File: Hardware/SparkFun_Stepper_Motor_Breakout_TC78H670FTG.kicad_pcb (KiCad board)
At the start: 4 copper layers, 15.2 x 20.3 mm, 44 parts, among them J1 Conn_01x08, J2 Conn_01x08, U1 TC78H670FTG

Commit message: version to v10
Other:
- board text added: "v10"
- board text removed: "v01"
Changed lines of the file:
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@@
     (effects (font (size 0.5 0.5) (thickness 0.1) bold) (justify left bottom))
   )
-  (gr_text "v01" (at 141.988553 94.318209 180) (layer "B.Cu")
+  (gr_text "v10" (at 141.988553 94.318209 180) (layer "B.Cu")
     (effects (font (size 1 1) (thickness 0.15)) (justify left bottom mirror))
   )

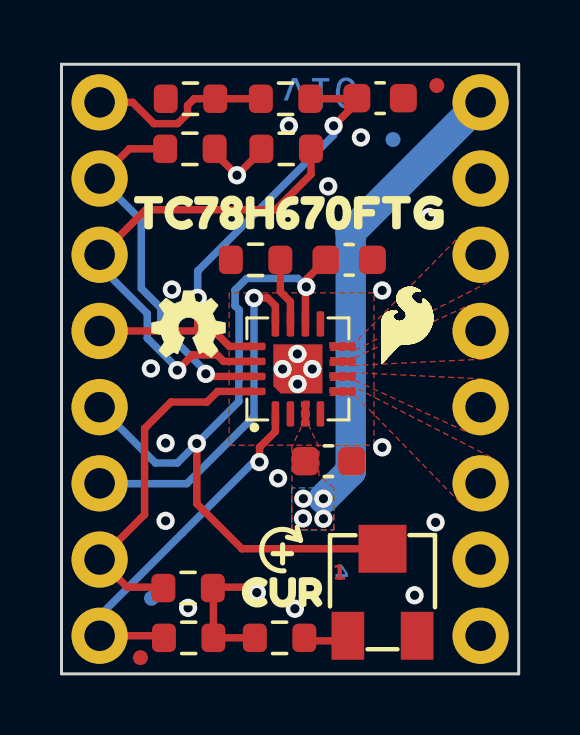
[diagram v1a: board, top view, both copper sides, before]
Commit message: library work and sch cleanup
-moved to a 0.05" grid for schematic and tightened things up (made all nets shorter to match smaller grid and only use a single grid space to extend out from any pin)
-updated ordering instructions fp to avoid sch->brd update error
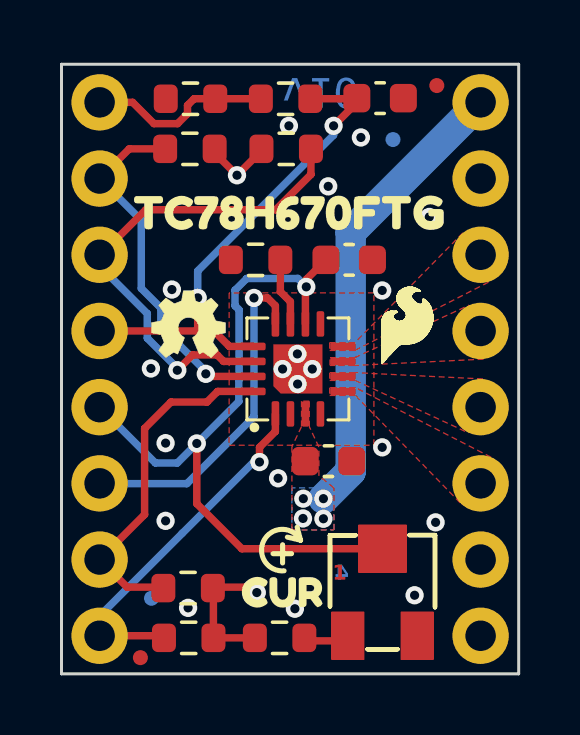
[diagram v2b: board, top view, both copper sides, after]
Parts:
- added R2: 10k, SparkFun-Resistor:Trimpot_SMD_3.0x3.0mm, F.Cu at (145.3, 111.6)
- J1: footprint SparkFun-Connector:1X08 -> SparkFun-Connector:1x08
- U2: footprint SparkFun-Aesthetic:ORDERING_INSTRUCTIONS -> SparkFun-Aesthetic:Ordering_Instructions
- moved U2 2.46 mm to (167.6, 58.5)
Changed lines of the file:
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@@
     )
   )
+  (footprint "SparkFun-Aesthetic:Ordering_Instructions" (layer "F.Cu")
+    (at 167.5642 58.505)
+    (property "Sheetfile" "SparkFun_Stepper_Motor_Breakout_TC78H670FTG.kicad_sch")
+    (property "Sheetname" "")
+    (fp_text reference "U2" (at 2.54 -1.27) (layer "F.Fab") hide
+        (effects (font (size 1.27 1.27) (thickness 0.15)))
+    )
+    (fp_text value "~" (at 2.54 -2.54) (layer "F.Fab") hide
+        (effects (font (size 1.27 1.27) (thickness 0.15)))
+    )
+    (fp_text user "Ordering Instructions:" (at 1.27 1.27) (layer "User.1")
+        (effects (font (size 2.5908 2.5908) (thickness 0.4572)) (justify left top))
+    )
+    (fp_line (start 0 4.445) (end 63.5 4.445)
+      (stroke (width 0.2032) (type solid)) (layer "User.1"))
+    (fp_rect (start 0 0) (end 63.5 50.8)
+      (stroke (width 0.2) (type default)) (fill none) (layer "User.1"))
+  )
   (footprint "SparkFun-Capacitor:C_0603_1608Metric" (layer "F.Cu")
     (at 145.24 95.11)
@@
     )
   )
-  (footprint "SparkFun-Aesthetic:ORDERING_INSTRUCTIONS" (layer "F.Cu")
-    (at 167.64 60.96)
-    (property "Sheetfile" "SparkFun_Stepper_Motor_Breakout_TC78H670FTG.kicad_sch")
-    (property "Sheetname" "")
-    (fp_text reference "U2" (at 2.54 -1.27) (layer "F.Fab") hide
-        (effects (font (size 1.27 1.27) (thickness 0.15)))
-    )
-    (fp_text value "~" (at 2.54 -2.54) (layer "F.Fab") hide
-        (effects (font (size 1.27 1.27) (thickness 0.15)))
-    )
-    (fp_text user "Ordering Instructions:" (at 1.27 1.27) (layer "User.1")
-        (effects (font (size 2.5908 2.5908) (thickness 0.4572)) (justify left top))
-    )
-    (fp_line (start 0 4.445) (end 63.5 4.445)
-      (stroke (width 0.2032) (type solid)) (layer "User.1"))
-    (fp_rect (start 0 0) (end 63.5 50.8)
-      (stroke (width 0.2) (type default)) (fill none) (layer "User.1"))
-  )
   (footprint "SparkFun-Capacitor:C_0603_1608Metric" (layer "F.Cu")
     (at 143.52 107.21)
@@
     )
   )
+  (footprint "SparkFun-Resistor:Trimpot_SMD_3.0x3.0mm" (layer "F.Cu")
+    (at 145.32 111.58)
+    (descr "https://www.ttelectronics.com/TTElectronics/media/ProductFiles/Datasheet/22.pdf")
+    (tags "Trimmer")
+    (property "Mfg Part#" "22AR10K")
+    (property "PROD_ID" "RES-09285")
+    (property "Sheetfile" "SparkFun_Stepper_Motor_Breakout_TC78H670FTG.kicad_sch")
+    (property "Sheetname" "")
+    (property "ki_description" "Potentiometer TRIMPOT-SMD-3MM-CLOSED-1/8W-20%")
+    (property "ki_keywords" "resistor variable trimmer")
+    (attr smd)
+    (fp_text reference "R2" (at 0 -2.8) (layer "F.Fab")
+        (effects (font (size 0.5 0.5) (thickness 0.1) bold))
+    )
+    (fp_text value "10k" (at 0.025 2.875) (layer "F.Fab")
+        (effects (font (size 0.5 0.5) (thickness 0.1) bold))
+    )
+    (fp_line (start -1.75 -1.9) (end -0.9 -1.9)
+      (stroke (width 0.15) (type default)) (layer "F.SilkS"))
+    (fp_line (start -1.75 0.475) (end -1.75 -1.9)
+      (stroke (width 0.15) (type default)) (layer "F.SilkS"))
+    (fp_line (start 0.5 1.9) (end -0.5 1.9)
+      (stroke (width 0.15) (type default)) (layer "F.SilkS"))
+    (fp_line (start 1.75 -1.905) (end 0.9 -1.905)
+      (stroke (width 0.15) (type default)) (layer "F.SilkS"))
+    (fp_line (start 1.75 0.5) (end 1.75 -1.9)
+      (stroke (width 0.15) (type default)) (layer "F.SilkS"))
+    (fp_rect (start -1.875 -2.37) (end 1.875 2.37)
+      (stroke (width 0.05) (type default)) (fill none) (layer "F.CrtYd"))
+    (fp_rect (start -1.6 -1.755) (end 1.6 1.755)
+      (stroke (width 0.1) (type solid)) (fill none) (layer "F.Fab"))
+    (pad "1" smd rect (at -1.155 1.45) (size 1.09 1.6) (layers "F.Cu" "F.Paste" "F.Mask")
+      (net 16 "Net-(R1-Pad2)") (pintype "passive") (thermal_bridge_angle 0))
+    (pad "2" smd rect (at 0 -1.45) (size 1.6 1.6) (layers "F.Cu" "F.Paste" "F.Mask")
+      (net 6 "VREF") (pintype "passive") (thermal_bridge_angle 0))
+    (pad "3" smd rect (at 1.155 1.45) (size 1.09 1.6) (layers "F.Cu" "F.Paste" "F.Mask")
+      (net 13 "GND") (pintype "passive") (thermal_bridge_angle 0))
+  )
   (footprint "SparkFun-Aesthetic:Creative_Commons_License" (layer "F.Cu")
     (at 0.25 0.25)
@@
       (stroke (width 0) (type solid)) (fill solid) (layer "F.SilkS"))
   )
-  (footprint "SparkFun-Connector:1X08" (layer "F.Cu")
+  (footprint "SparkFun-Connector:1x08" (layer "F.Cu")
     (at 135.89 95.25 -90)
     (property "Sheetfile" "SparkFun_Stepper_Motor_Breakout_TC78H670FTG.kicad_sch")
@@
     (property "ki_description" "Generic connector, single row, 01x08, script generated (kicad-library-utils/schlib/autogen/connector/)")
     (property "ki_keywords" "connector")
-    (fp_text reference "J1" (at -1.27 -1.397 90) (layer "F.Fab")
-        (effects (font (size 0.5 0.5) (thickness 0.1)) (justify right bottom))
+    (fp_text reference "J1" (at -1.27 -1.397 -90) (layer "F.Fab")
+        (effects (font (size 0.5 0.5) (thickness 0.1)) (justify left bottom))
     )
-    (fp_text value "Conn_01x08" (at -1.016 1.778 90) (layer "F.Fab")
-        (effects (font (size 0.5 0.5) (thickness 0.1)) (justify right bottom))
+    (fp_text value "Conn_01x08" (at -1.27 2.032 -90) (layer "F.Fab")
+        (effects (font (size 0.5 0.5) (thickness 0.1)) (justify left bottom))
     )
     (fp_poly
@@
   (via (at 138.3 101.49) (size 0.6096) (drill 0.3048) (layers "F.Cu" "B.Cu") (net 13))
   (via (at 142.49 104.64) (size 0.6096) (drill 0.3048) (layers "F.Cu" "B.Cu") (net 13))
-  (via (at 146.39 111.68) (size 0.6096) (drill 0.3048) (layers "F.Cu" "B.Cu") (net 13))
+  (via (at 146.39 111.68) (size 0.6096) (drill 0.3048) (layers "F.Cu" "B.Cu") (free) (net 13))
   (via (at 145.31 106.75) (size 0.6096) (drill 0.3048) (layers "F.Cu" "B.Cu") (net 13))
   (via (at 144.6 96.42) (size 0.6096) (drill 0.3048) (layers "F.Cu" "B.Cu") (net 13))

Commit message: removing duplicate trimpot in PCB file
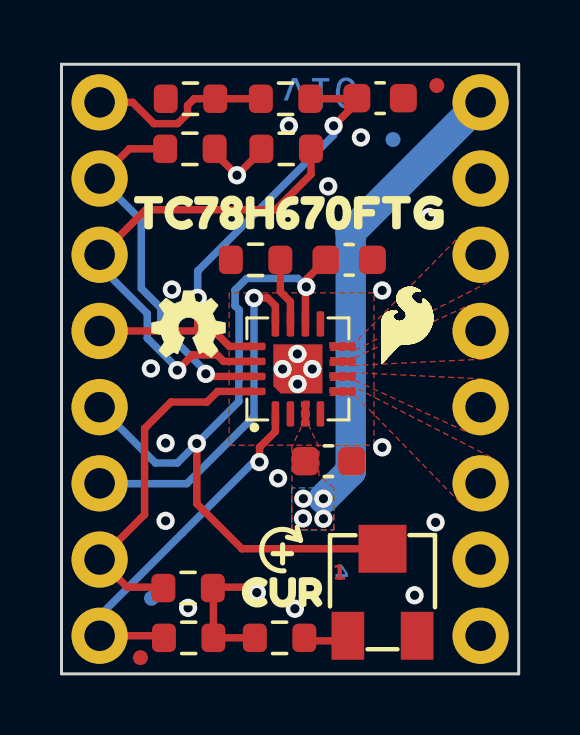
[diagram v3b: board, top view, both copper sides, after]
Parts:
- removed RV1: 10K, SparkFun-Resistor:Trimpot_SMD_3.0x3.0mm
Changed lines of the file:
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@@
   (net 14 "ERR")
   (net 15 "EN")
-  (net 16 "Net-(R1-Pad2)")
-  (net 17 "Net-(U1-OSCM)")
+  (net 16 "Net-(U1-OSCM)")
+  (net 17 "Net-(R1-Pad2)")
   (footprint "kibuzzard-65D531EE" (layer "F.Cu")
     (at 141.98 111.58)
@@
     )
   )
+  (footprint "SparkFun-Resistor:Trimpot_SMD_3.0x3.0mm" (layer "F.Cu")
+    (at 145.32 111.58)
+    (descr "https://www.ttelectronics.com/TTElectronics/media/ProductFiles/Datasheet/22.pdf")
+    (tags "Trimmer")
+    (property "Mfg Part#" "22AR10K")
+    (property "PROD_ID" "RES-09285")
+    (property "Sheetfile" "SparkFun_Stepper_Motor_Breakout_TC78H670FTG.kicad_sch")
+    (property "Sheetname" "")
+    (property "ki_description" "Potentiometer TRIMPOT-SMD-3MM-CLOSED-1/8W-20%")
+    (property "ki_keywords" "resistor variable trimmer")
+    (attr smd)
+    (fp_text reference "R2" (at 0 -2.8) (layer "F.Fab")
+        (effects (font (size 0.5 0.5) (thickness 0.1) bold))
+    )
+    (fp_text value "10k" (at 0.025 2.875) (layer "F.Fab")
+        (effects (font (size 0.5 0.5) (thickness 0.1) bold))
+    )
+    (fp_line (start -1.75 -1.9) (end -0.9 -1.9)
+      (stroke (width 0.15) (type default)) (layer "F.SilkS"))
+    (fp_line (start -1.75 0.475) (end -1.75 -1.9)
+      (stroke (width 0.15) (type default)) (layer "F.SilkS"))
+    (fp_line (start 0.5 1.9) (end -0.5 1.9)
+      (stroke (width 0.15) (type default)) (layer "F.SilkS"))
+    (fp_line (start 1.75 -1.905) (end 0.9 -1.905)
+      (stroke (width 0.15) (type default)) (layer "F.SilkS"))
+    (fp_line (start 1.75 0.5) (end 1.75 -1.9)
+      (stroke (width 0.15) (type default)) (layer "F.SilkS"))
+    (fp_rect (start -1.875 -2.37) (end 1.875 2.37)
+      (stroke (width 0.05) (type default)) (fill none) (layer "F.CrtYd"))
+    (fp_rect (start -1.6 -1.755) (end 1.6 1.755)
+      (stroke (width 0.1) (type solid)) (fill none) (layer "F.Fab"))
+    (pad "1" smd rect (at -1.155 1.45) (size 1.09 1.6) (layers "F.Cu" "F.Paste" "F.Mask")
+      (net 17 "Net-(R1-Pad2)") (pintype "passive") (thermal_bridge_angle 0))
+    (pad "2" smd rect (at 0 -1.45) (size 1.6 1.6) (layers "F.Cu" "F.Paste" "F.Mask")
+      (net 6 "VREF") (pintype "passive") (thermal_bridge_angle 0))
+    (pad "3" smd rect (at 1.155 1.45) (size 1.09 1.6) (layers "F.Cu" "F.Paste" "F.Mask")
+      (net 13 "GND") (pintype "passive") (thermal_bridge_angle 0))
+  )
   (footprint "SparkFun-Capacitor:C_0603_1608Metric" (layer "F.Cu")
     (at 144.21 100.5)
@@
       (stroke (width 0.1) (type solid)) (layer "F.Fab"))
     (pad "1" smd roundrect (at -0.825 0 180) (size 0.8 0.95) (layers "F.Cu" "F.Paste" "F.Mask") (roundrect_rratio 0.25)
-      (net 17 "Net-(U1-OSCM)") (pintype "passive"))
+      (net 16 "Net-(U1-OSCM)") (pintype "passive"))
     (pad "2" smd roundrect (at 0.825 0 180) (size 0.8 0.95) (layers "F.Cu" "F.Paste" "F.Mask") (roundrect_rratio 0.25)
       (net 13 "GND") (pintype "passive"))
@@
     )
   )
-  (footprint "SparkFun-Resistor:Trimpot_SMD_3.0x3.0mm" (layer "F.Cu")
-    (at 145.32 111.58)
-    (property "PROD_ID" "RES-09285")
-    (property "Sheetfile" "SparkFun_Stepper_Motor_Carrier_TC78H670FTG.kicad_sch")
-    (property "Sheetname" "")
-    (property "ki_description" "Potentiometer")
-    (property "ki_keywords" "resistor variable")
-    (attr smd)
-    (fp_text reference "RV1" (at 0 -2.8) (layer "F.Fab")
-        (effects (font (size 0.5 0.5) (thickness 0.1) bold))
-    )
-    (fp_text value "10K" (at 0.025 2.875) (layer "F.Fab")
-        (effects (font (size 0.5 0.5) (thickness 0.1) bold))
-    )
-    (fp_line (start -1.75 -1.9) (end -0.9 -1.9)
-      (stroke (width 0.15) (type default)) (layer "F.SilkS"))
-    (fp_line (start -1.75 0.475) (end -1.75 -1.9)
-      (stroke (width 0.15) (type default)) (layer "F.SilkS"))
-    (fp_line (start 0.5 1.9) (end -0.5 1.9)
-      (stroke (width 0.15) (type default)) (layer "F.SilkS"))
-    (fp_line (start 1.75 -1.905) (end 0.9 -1.905)
-      (stroke (width 0.15) (type default)) (layer "F.SilkS"))
-    (fp_line (start 1.75 0.5) (end 1.75 -1.9)
-      (stroke (width 0.15) (type default)) (layer "F.SilkS"))
-    (fp_rect (start -1.875 -2.37) (end 1.875 2.37)
-      (stroke (width 0.05) (type default)) (fill none) (layer "F.CrtYd"))
-    (fp_rect (start -1.6 -1.755) (end 1.6 1.755)
-      (stroke (width 0.1) (type solid)) (fill none) (layer "F.Fab"))
-    (pad "1" smd rect (at -1.155 1.45) (size 1.09 1.6) (layers "F.Cu" "F.Paste" "F.Mask")
-      (net 16 "Net-(R1-Pad2)") (pintype "passive") (thermal_bridge_angle 0))
-    (pad "2" smd rect (at 0 -1.45) (size 1.6 1.6) (layers "F.Cu" "F.Paste" "F.Mask")
-      (net 6 "VREF") (pintype "passive") (thermal_bridge_angle 0))
-    (pad "3" smd rect (at 1.155 1.45) (size 1.09 1.6) (layers "F.Cu" "F.Paste" "F.Mask")
-      (net 13 "GND") (pintype "passive") (thermal_bridge_angle 0))
-  )
   (footprint "SparkFun-Aesthetic:SFE_FLAME_0.1" (layer "F.Cu")
     (at 146.101859 102.734273)
@@
       (net 6 "VREF") (pinfunction "VREF") (pintype "bidirectional") (thermal_bridge_angle 45))
     (pad "11" smd roundrect (at 1 3 180) (size 0.255 0.85) (layers "F.Cu" "F.Mask") (roundrect_rratio 0.25)
-      (net 17 "Net-(U1-OSCM)") (pinfunction "OSCM") (pintype "bidirectional") (thermal_bridge_angle 45))
+      (net 16 "Net-(U1-OSCM)") (pinfunction "OSCM") (pintype "bidirectional") (thermal_bridge_angle 45))
     (pad "12" smd roundrect (at 1.5 3 180) (size 0.255 0.85) (layers "F.Cu" "F.Mask") (roundrect_rratio 0.25)
       (net 7 "~{STBY}") (pinfunction "STBY") (pintype "input") (thermal_bridge_angle 45))
@@
       (net 8 "3.3V") (pintype "passive"))
     (pad "2" smd roundrect (at 0.825 0) (size 0.8 0.95) (layers "F.Cu" "F.Paste" "F.Mask") (roundrect_rratio 0.25)
-      (net 16 "Net-(R1-Pad2)") (pintype "passive"))
+      (net 17 "Net-(R1-Pad2)") (pintype "passive"))
     (model "${KICAD6_3DMODEL_DIR}/Resistor_SMD.3dshapes/R_0603_1608Metric.wrl"
       (offset (xyz 0 0 0))
@@
     )
   )
-  (footprint "SparkFun-Resistor:Trimpot_SMD_3.0x3.0mm" (layer "F.Cu")
-    (at 145.32 111.58)
-    (descr "https://www.ttelectronics.com/TTElectronics/media/ProductFiles/Datasheet/22.pdf")
-    (tags "Trimmer")
-    (property "Mfg Part#" "22AR10K")
-    (property "PROD_ID" "RES-09285")
-    (property "Sheetfile" "SparkFun_Stepper_Motor_Breakout_TC78H670FTG.kicad_sch")
-    (property "Sheetname" "")
-    (property "ki_description" "Potentiometer TRIMPOT-SMD-3MM-CLOSED-1/8W-20%")
-    (property "ki_keywords" "resistor variable trimmer")
-    (attr smd)
-    (fp_text reference "R2" (at 0 -2.8) (layer "F.Fab")
-        (effects (font (size 0.5 0.5) (thickness 0.1) bold))
-    )
-    (fp_text value "10k" (at 0.025 2.875) (layer "F.Fab")
-        (effects (font (size 0.5 0.5) (thickness 0.1) bold))
-    )
-    (fp_line (start -1.75 -1.9) (end -0.9 -1.9)
-      (stroke (width 0.15) (type default)) (layer "F.SilkS"))
-    (fp_line (start -1.75 0.475) (end -1.75 -1.9)
-      (stroke (width 0.15) (type default)) (layer "F.SilkS"))
-    (fp_line (start 0.5 1.9) (end -0.5 1.9)
-      (stroke (width 0.15) (type default)) (layer "F.SilkS"))
-    (fp_line (start 1.75 -1.905) (end 0.9 -1.905)
-      (stroke (width 0.15) (type default)) (layer "F.SilkS"))
-    (fp_line (start 1.75 0.5) (end 1.75 -1.9)
-      (stroke (width 0.15) (type default)) (layer "F.SilkS"))
-    (fp_rect (start -1.875 -2.37) (end 1.875 2.37)
-      (stroke (width 0.05) (type default)) (fill none) (layer "F.CrtYd"))
-    (fp_rect (start -1.6 -1.755) (end 1.6 1.755)
-      (stroke (width 0.1) (type solid)) (fill none) (layer "F.Fab"))
-    (pad "1" smd rect (at -1.155 1.45) (size 1.09 1.6) (layers "F.Cu" "F.Paste" "F.Mask")
-      (net 16 "Net-(R1-Pad2)") (pintype "passive") (thermal_bridge_angle 0))
-    (pad "2" smd rect (at 0 -1.45) (size 1.6 1.6) (layers "F.Cu" "F.Paste" "F.Mask")
-      (net 6 "VREF") (pintype "passive") (thermal_bridge_angle 0))
-    (pad "3" smd rect (at 1.155 1.45) (size 1.09 1.6) (layers "F.Cu" "F.Paste" "F.Mask")
-      (net 13 "GND") (pintype "passive") (thermal_bridge_angle 0))
-  )
   (footprint "SparkFun-Aesthetic:Creative_Commons_License" (layer "F.Cu")
     (at 0.25 0.25)
@@
   (segment (start 136.991996 95.25) (end 135.89 95.25) (width 0.25) (layer "F.Cu") (net 15))
   (segment (start 138.82 95.628004) (end 138.488004 95.96) (width 0.25) (layer "F.Cu") (net 15))
-  (segment (start 144.58 113.2) (end 143.005 113.2) (width 0.25) (layer "F.Cu") (net 16))
-  (segment (start 143.005 113.2) (end 142.895 113.09) (width 0.25) (layer "F.Cu") (net 16))
-  (segment (start 141.915 101.560305) (end 141.915 100.5) (width 0.25) (layer "F.Cu") (net 17))
-  (segment (start 142.25 101.895305) (end 141.915 101.560305) (width 0.25) (layer "F.Cu") (net 17))
-  (segment (start 142.25 102.636025) (end 142.25 101.895305) (width 0.25) (layer "F.Cu") (net 17))
+  (segment (start 141.915 101.560305) (end 141.915 100.5) (width 0.25) (layer "F.Cu") (net 16))
+  (segment (start 142.25 101.895305) (end 141.915 101.560305) (width 0.25) (layer "F.Cu") (net 16))
+  (segment (start 142.25 102.636025) (end 142.25 101.895305) (width 0.25) (layer "F.Cu") (net 16))
+  (segment (start 144.58 113.2) (end 143.005 113.2) (width 0.25) (layer "F.Cu") (net 17))
+  (segment (start 143.005 113.2) (end 142.895 113.09) (width 0.25) (layer "F.Cu") (net 17))
   (zone (net 5) (net_name "VM") (layer "F.Cu") (name "VM") (hatch edge 0.5)
     (priority 2)
